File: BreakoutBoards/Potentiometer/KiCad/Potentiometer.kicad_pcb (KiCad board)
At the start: 2 copper layers, 14.7 x 21 mm, 3 parts, among them J1 Conn_01x03_Pin

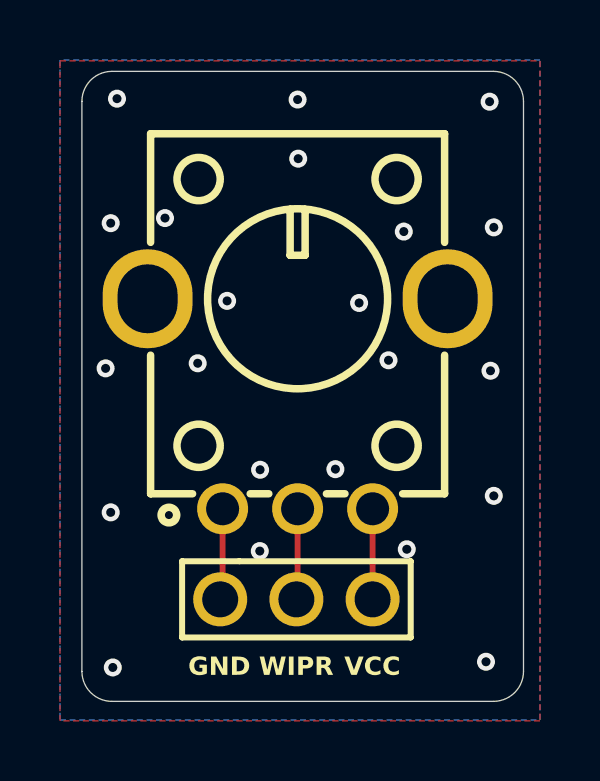
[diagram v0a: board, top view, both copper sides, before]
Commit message: ran DRC and resolved issues
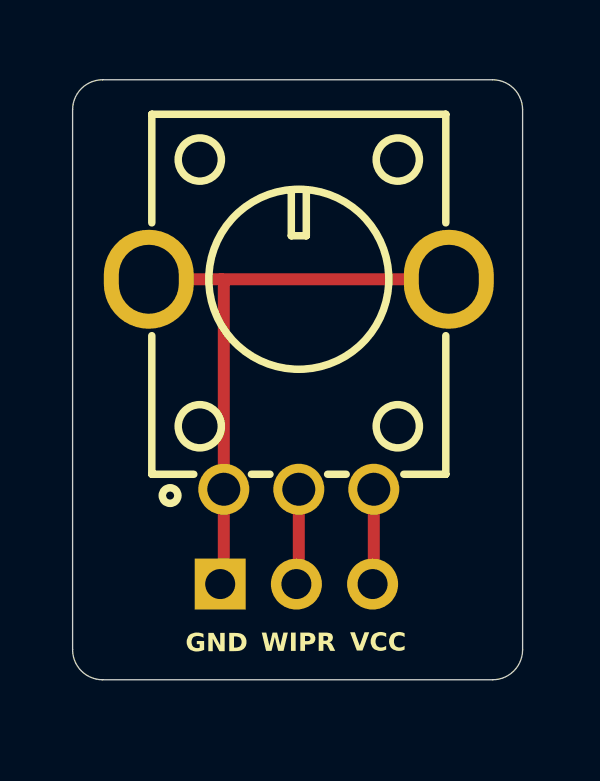
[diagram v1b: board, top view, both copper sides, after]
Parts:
- J1: footprint clectric-diy:HDR-TH_3P-P2.54-V-M-1 -> Connector_PinHeader_2.54mm:PinHeader_1x03_P2.54mm_Vertical; moved to B.Cu
- R1: value RK09KXXXXXXX -> RK09K1130D62
- moved J1 2.59 mm to (116.8, 107.4), turned to -90 degrees
- moved G*** 1.22 mm to (119.5, 93.9)
- moved R1 0.65 mm to (119.5, 100.8)
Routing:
- net GND+CCW: track 3.05 -> 20.2 mm, vias 22 -> 0
- removed copper zone on B.Cu, net GND+CCW
- removed copper zone on F.Cu, net GND+CCW
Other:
- board size 14.7 x 21 mm -> 15 x 20 mm

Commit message: updated to Mk1 and sent for manufacturing
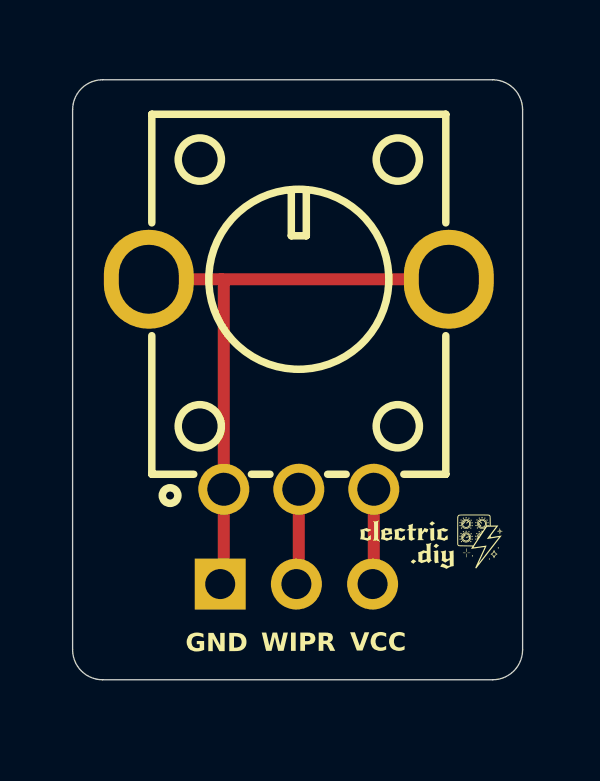
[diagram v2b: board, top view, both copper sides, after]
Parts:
- added G***: LOGO, clectric-diy-branding:clectric.diy-Wordmark-5mm, F.Cu at (123.9, 106.0)
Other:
- board text added: "Charge Potentiometer Mk1"
- board text removed: "Charge Potentiometer Mk 0.1"
